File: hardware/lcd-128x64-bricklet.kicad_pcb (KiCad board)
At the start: 2 copper layers, 95 x 55 mm, 34 parts, among them P1 CON-SENSOR2, P2 Debug, P3 BOOT, P4 CON_4Wire_ER-TP028-1, Q1 2N7002, U1 XMC130024, U2 TSC2046E, U3 LCD-ERC12864, U4 DRILL, U5 DRILL, U6 DRILL, U7 DRILL

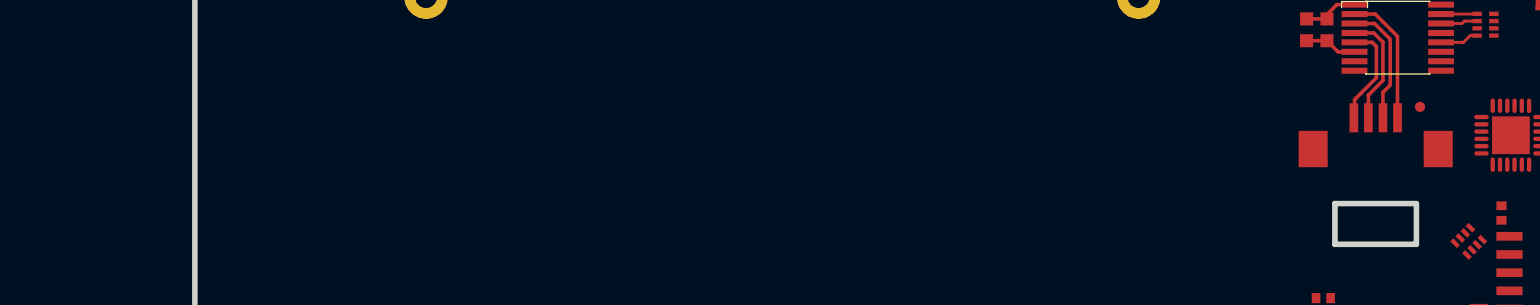
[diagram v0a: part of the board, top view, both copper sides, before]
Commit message: add drawing of touchscreen cable
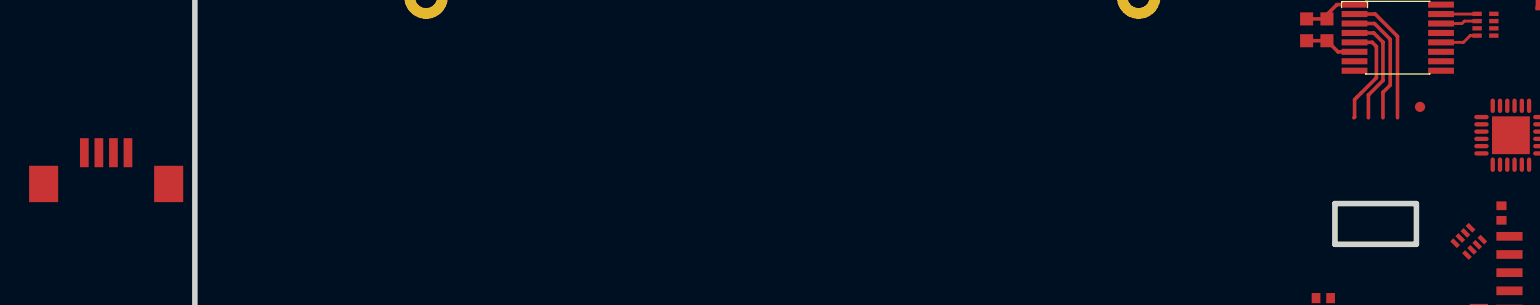
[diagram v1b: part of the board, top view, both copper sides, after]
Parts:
- moved P4 87.3 mm to (92.9, 79.3)
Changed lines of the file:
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@@
-(kicad_pcb (version 4) (host pcbnew 4.0.2+dfsg1-stable)
+(kicad_pcb (version 4) (host pcbnew 4.0.7-e2-6376~58~ubuntu17.04.1)
   (general
     (links 98)
-    (no_connects 62)
-    (area 98.809499 61.109499 194.190501 116.490501)
+    (no_connects 66)
+    (area 98.094999 60.394999 194.905001 117.205001)
     (thickness 1.6)
-    (drawings 13)
+    (drawings 17)
     (tracks 82)
     (zones 0)
@@
   )
   (setup
-    (last_trace_width 0.2)
+    (last_trace_width 0.25)
     (user_trace_width 0.2)
     (user_trace_width 0.25)
@@
   )
   (module kicad-libraries:ER-CON04HB-2 (layer F.Cu)
-    (at 180.2 76.9)
+    (at 92.9 79.3)
     (fp_text reference P4 (at 0 2.03) (layer F.Fab)
       (effects (font (size 0.15 0.15) (thickness 0.0375)))
@@
     )
   )
+  (gr_line (start 93 76.4) (end 93.6 76.4) (angle 90) (layer Dwgs.User) (width 0.381))
+  (gr_line (start 92.7 97.1) (end 93 76.4) (angle 90) (layer Dwgs.User) (width 0.381))
+  (gr_line (start 114.6 34.9) (end 92.7 97.1) (angle 90) (layer Dwgs.User) (width 0.381))
+  (gr_line (start 114.6 71.7) (end 114.6 34.9) (angle 90) (layer Dwgs.User) (width 0.381))
   (gr_text status (at 180.18 111.53) (layer F.SilkS)
     (effects (font (size 1 1) (thickness 0.15)))

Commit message: Complete routing
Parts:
- added G***: Logo_31x31, kicad-libraries:Logo_31x31, F.Cu at (178.9, 102.9)
- added G***: LOGO, kicad-libraries:Logo_CoMCU, B.Cu at (139.4, 88.8)
- added VAL: WEEE_7mm, kicad-libraries:WEEE_7mm, B.Cu at (127.6, 88.8)
- added VAL: CE_5mm, kicad-libraries:CE_5mm, B.Cu at (149.9, 88.8)
- moved U2 82.4 mm to (99.3, 69.5)
- moved C6 82.3 mm to (94.6, 68.8)
- moved C5 82.2 mm to (93.3, 68.8)
- moved R1 37.7 mm to (185.3, 76.4), turned to 270 degrees
- moved D1 34.0 mm to (185.3, 79.6), turned to 90 degrees
- moved C4 29.3 mm to (179.6, 68.5), turned to 180 degrees
- moved RP2 13.5 mm to (175.8, 76.8)
- moved U1 11.9 mm to (179.1, 72.3)
- moved Q1 11.9 mm to (176.6, 66.8), turned to 180 degrees
- moved R7 10.9 mm to (175.9, 78.5), turned to 180 degrees
- moved P3 8.78 mm to (183.8, 72.1), turned to 180 degrees
- moved RP1 7.75 mm to (178.8, 85.5)
- moved P4 7.68 mm to (98.4, 73.9)
- moved R4 7.43 mm to (159.6, 64.2), turned to 0 degrees
- moved R6 7.43 mm to (152.1, 63.8)
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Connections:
- R7 pad 2: M-CS-LCD -> M-MOSI
- RP2 pad 2: M-MISO -> M-CS-LCD
- U1 pad 1: Net-(RP2-Pad7) -> Net-(R7-Pad1)
- U1 pad 15: Net-(P2-Pad1) -> Net-(U1-Pad15)
- U1 pad 2: Net-(U1-Pad2) -> Net-(P2-Pad1)
- U1 pad 22: Net-(R7-Pad1) -> Net-(RP2-Pad7)
- U2 pad 14: M-MISO -> M-MOSI
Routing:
- net VCC: track 16.6 -> 244.5 mm, vias 0 -> 4
- net M-CLK: track 0.00 -> 83.3 mm
- net TS-BUSY: track 0.00 -> 82.3 mm, vias 0 -> 4
- net PENIRQ: track 0.00 -> 79.0 mm, vias 0 -> 2
- net M-MISO: track 5.22 -> 82.9 mm, vias 0 -> 2
- net M-MOSI: track 0.00 -> 77.1 mm, vias 0 -> 2
- net M-CS-TS: track 2.49 -> 76.7 mm, vias 0 -> 4
- net LCD-RST: track 0.00 -> 56.8 mm, vias 0 -> 2
- net M-CS-LCD: track 0.00 -> 54.2 mm, vias 0 -> 2
- net LCD-CD: track 0.00 -> 51.9 mm, vias 0 -> 4
- net GND: track 13.0 -> 38.4 mm, vias 3 -> 17
- net S-MOSI: track 0.00 -> 14.0 mm, vias 0 -> 2
- net S-CS: track 0.00 -> 12.4 mm, vias 0 -> 2
- net S-MISO: track 0.00 -> 12.2 mm, vias 0 -> 2
- net S-CLK: track 0.00 -> 11.5 mm, vias 0 -> 2
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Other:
- outline, holes or cut-outs redrawn
- board text added: "LCD 128x64 1.0"
- board text added: "tinkerforge.com"

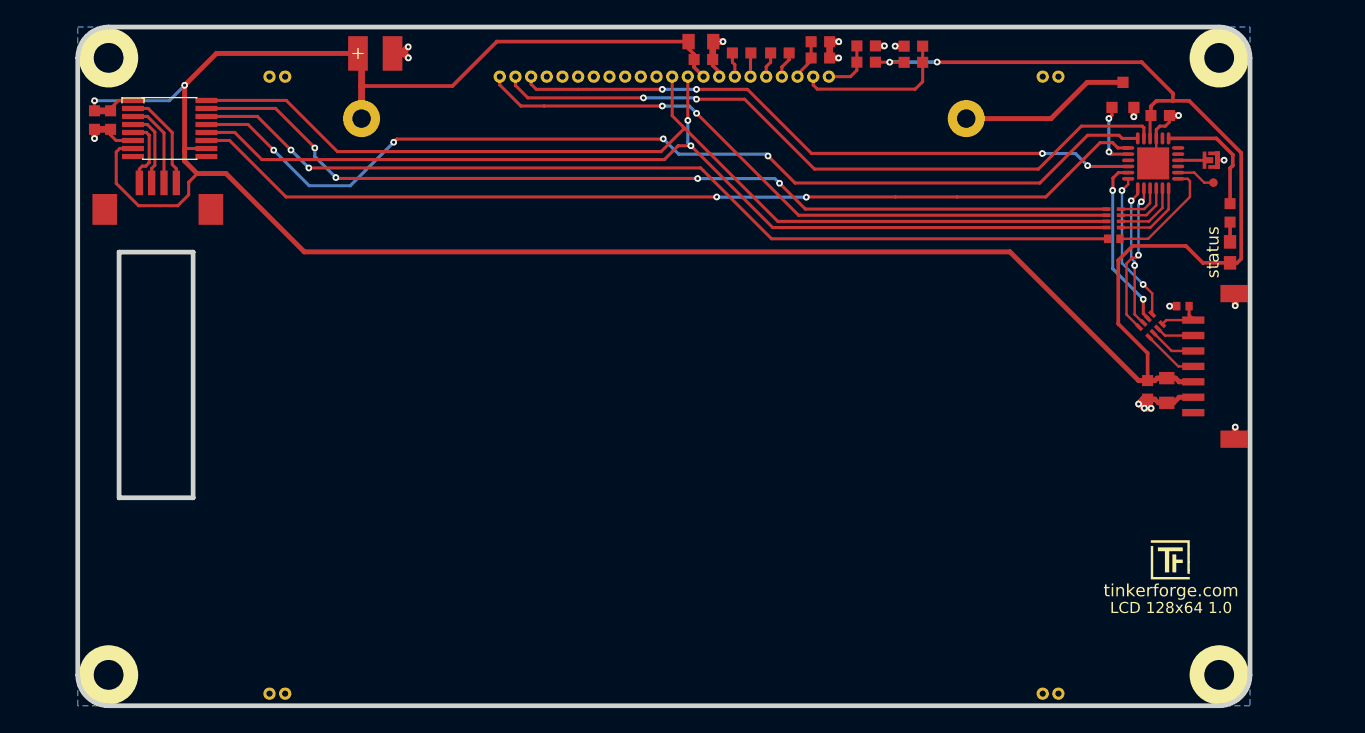
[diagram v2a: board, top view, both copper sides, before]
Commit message: add fiducials, destroy layout
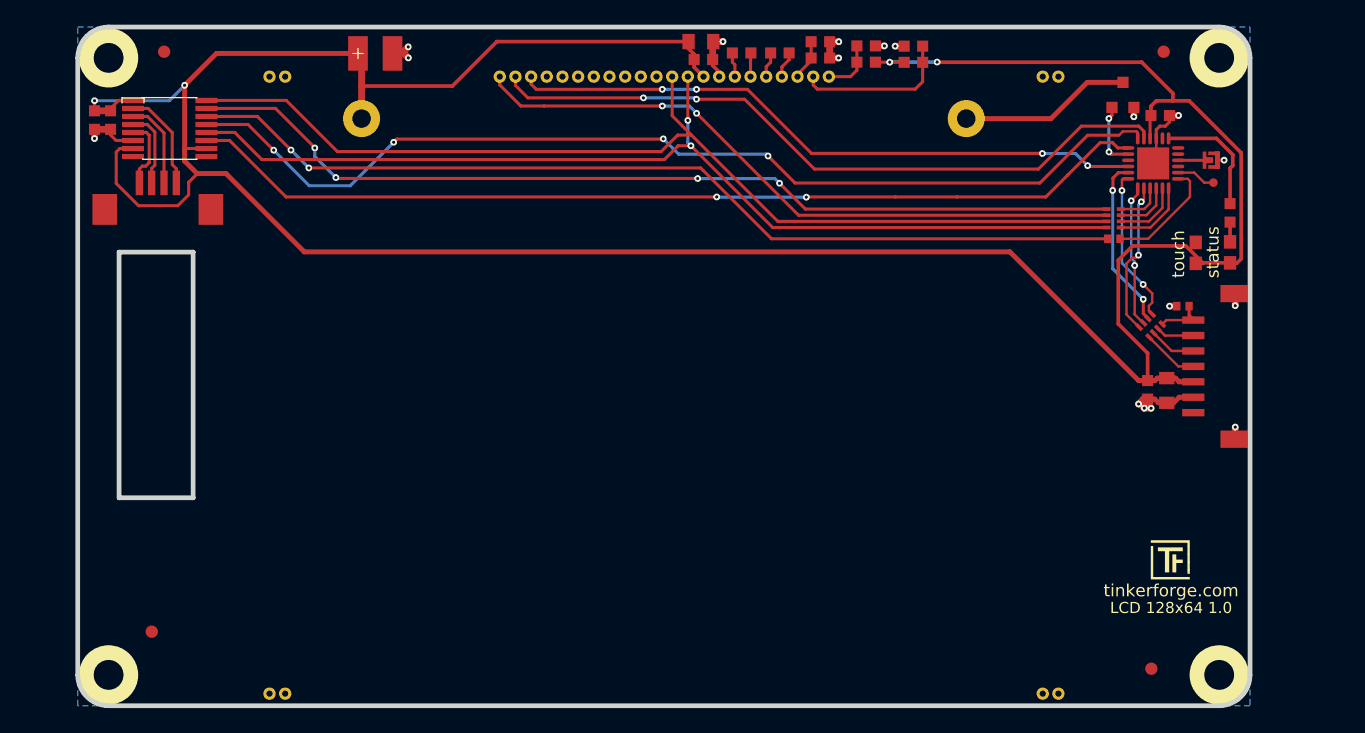
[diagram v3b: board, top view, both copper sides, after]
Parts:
- added D1: blue, kicad-libraries:D0603E, F.Cu at (182.5, 79.6)
- added Fiducial_Mark: VAL**, kicad-libraries:Fiducial_Mark, F.Cu at (97.9, 110.3)
- added Fiducial_Mark: VAL**, kicad-libraries:Fiducial_Mark, F.Cu at (178.9, 113.3)
- added Fiducial_Mark: VAL**, kicad-libraries:Fiducial_Mark, F.Cu at (98.9, 63.3)
- added Fiducial_Mark: VAL**, kicad-libraries:Fiducial_Mark, F.Cu at (179.9, 63.3)
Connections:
- P1 pad 1: Net-(P1-Pad1) -> (no net)
- U1 pad 15: Net-(U1-Pad15) -> (no net)
- U1 pad 3: Net-(U1-Pad3) -> (no net)
- U1 pad 5: Net-(U1-Pad5) -> (no net)
- U1 pad 6: Net-(U1-Pad6) -> (no net)
- U1 pad 8: Net-(U1-Pad8) -> (no net)
- U2 pad 8: Net-(U2-Pad8) -> (no net)
- U2 pad 9: Net-(U2-Pad9) -> (no net)
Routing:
- net TS-BUSY: track 82.3 -> 82.8 mm
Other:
- board text added: "touch"

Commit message: Add status LED for touch
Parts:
- removed the D1 at (182.5, 79.6)
- added D2: green, kicad-libraries:D0603E, F.Cu at (182.5, 79.6)
- added R8: 1k, kicad-libraries:R0603F, F.Cu at (183.0, 76.5)
- moved P2 9.16 mm to (175.0, 71.9)
- moved C1 1.52 mm to (180.0, 84.4), turned to 135 degrees
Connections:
- P1 pad 1: (no net) -> Net-(P1-Pad1)
- U1 pad 15: (no net) -> Net-(P2-Pad1)
- U1 pad 2: Net-(P2-Pad1) -> Net-(R8-Pad1)
- U1 pad 3: (no net) -> Net-(U1-Pad3)
- U1 pad 5: (no net) -> Net-(U1-Pad5)
- U1 pad 6: (no net) -> Net-(U1-Pad6)
- U1 pad 8: (no net) -> Net-(U1-Pad8)
- U2 pad 8: (no net) -> Net-(U2-Pad8)
- U2 pad 9: (no net) -> Net-(U2-Pad9)
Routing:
- net GND: track 38.4 -> 45.2 mm, vias 17 -> 21
- net Net-(R8-Pad1): track 0.00 -> 5.22 mm
- net Net-(D2-Pad2): track 0.00 -> 2.28 mm
- net VCC: track 244.5 -> 246.1 mm
- net Net-(C1-Pad1): track 4.08 -> 5.21 mm
- net Net-(P2-Pad1): track 3.19 -> 2.11 mm

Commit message: Recover routing
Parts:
- C5: footprint kicad-libraries:C0603F -> kicad-libraries:C0805
- moved C5 9.95 mm to (102.2, 73.2), turned to 0 degrees
- moved C6 1.07 mm to (93.5, 69.0)
- moved U2 0.71 mm to (98.7, 69.7)
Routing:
- net VCC: track 246.1 -> 234.2 mm, vias 4 -> 6
- net Net-(P4-Pad1): track 8.21 -> 8.82 mm
- net M-CLK: track 83.6 -> 84.2 mm
- net PENIRQ: track 79.0 -> 79.5 mm
- net GND: track 45.2 -> 45.1 mm, vias 21 -> 22

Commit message: some small layout improvements
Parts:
- moved P2 0.57 mm to (175.1, 72.5)
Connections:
- P1 pad 1: Net-(P1-Pad1) -> (no net)
- U1 pad 3: Net-(U1-Pad3) -> (no net)
- U1 pad 5: Net-(U1-Pad5) -> (no net)
- U1 pad 6: Net-(U1-Pad6) -> (no net)
- U1 pad 8: Net-(U1-Pad8) -> (no net)
- U2 pad 8: Net-(U2-Pad8) -> (no net)
- U2 pad 9: Net-(U2-Pad9) -> (no net)
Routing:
- net TS-BUSY: track 83.3 -> 81.1 mm
- net Net-(C1-Pad1): track 5.21 -> 3.24 mm
- net LCD-CD: track 51.9 -> 52.5 mm
- added copper zone on F.Cu, net GND
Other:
- net class Default: clearance 0.2 -> 0.15
- rule trace_clearance: 0.2 -> 0.15

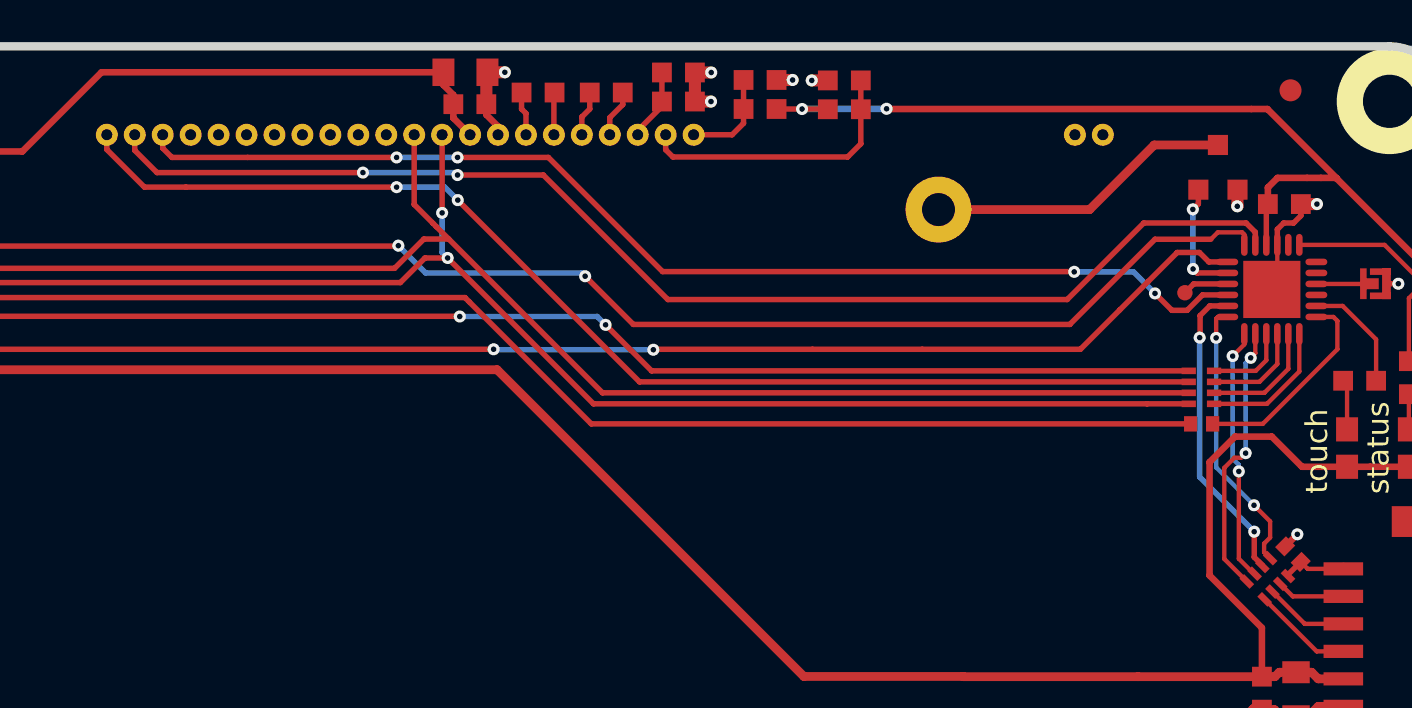
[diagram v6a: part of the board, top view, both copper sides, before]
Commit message: Change pins P1.3 with P0.8
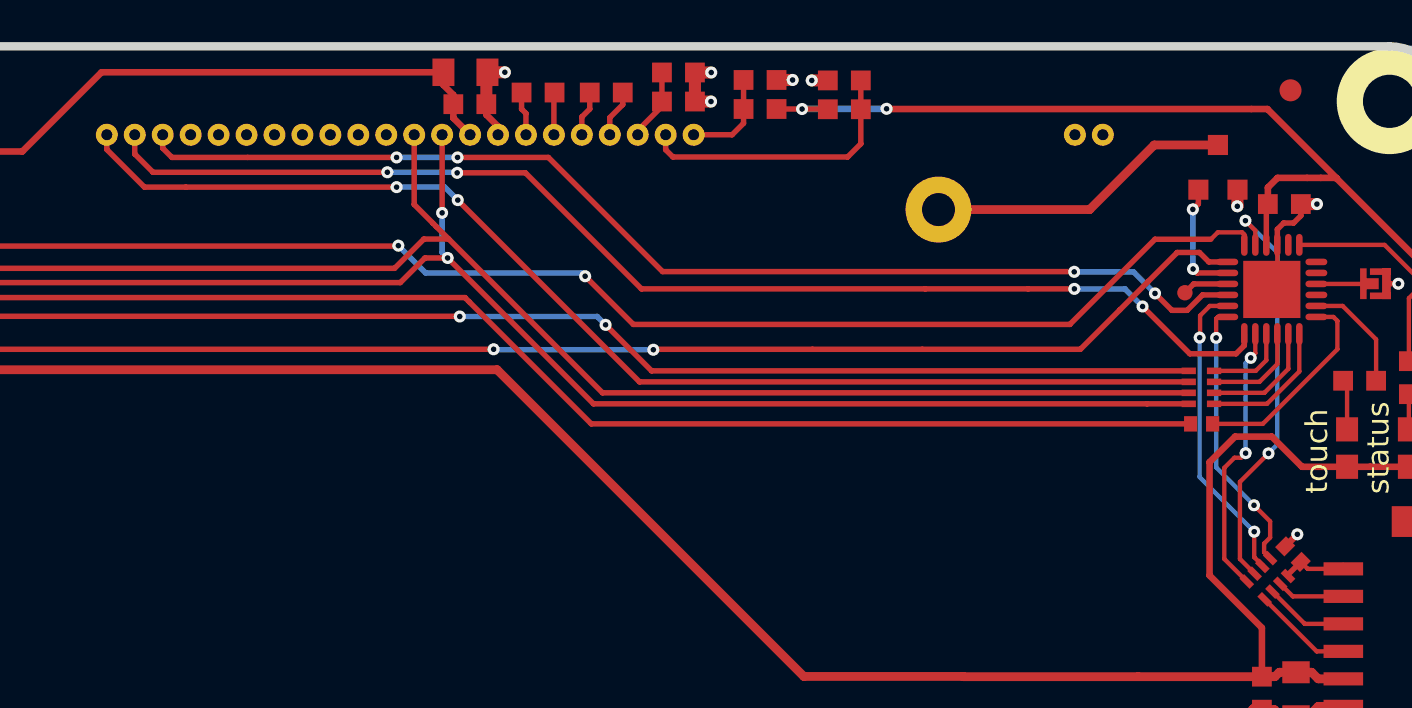
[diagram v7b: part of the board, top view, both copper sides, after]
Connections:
- P1 pad 1: (no net) -> Net-(P1-Pad1)
- U1 pad 11: LCD-RST -> S-CLK
- U1 pad 19: S-CLK -> LCD-RST
- U1 pad 3: (no net) -> Net-(U1-Pad3)
- U1 pad 5: (no net) -> Net-(U1-Pad5)
- U1 pad 6: (no net) -> Net-(U1-Pad6)
- U1 pad 8: (no net) -> Net-(U1-Pad8)
- U2 pad 8: (no net) -> Net-(U2-Pad8)
- U2 pad 9: (no net) -> Net-(U2-Pad9)
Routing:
- net S-CLK: track 11.5 -> 19.0 mm
- net LCD-RST: track 56.6 -> 55.7 mm, vias 2 -> 4
